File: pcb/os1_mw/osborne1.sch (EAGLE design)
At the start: 19 parts

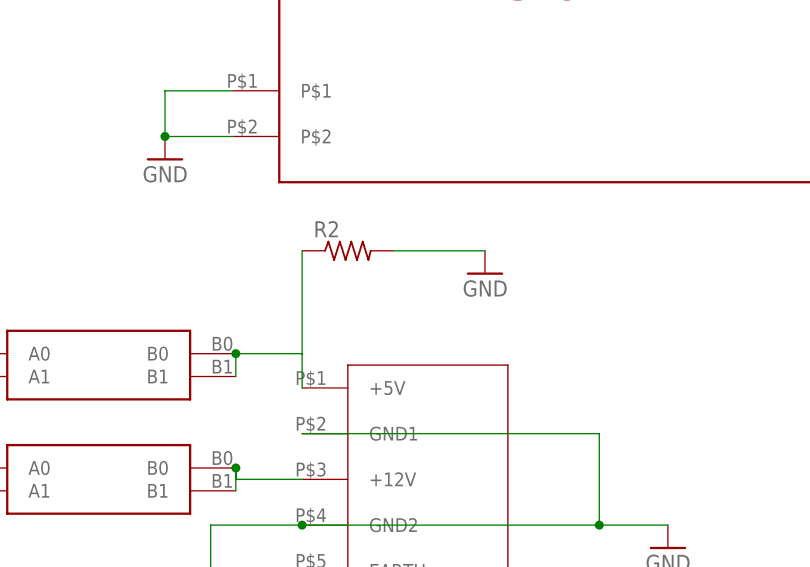
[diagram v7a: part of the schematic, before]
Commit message: update os1 pcb
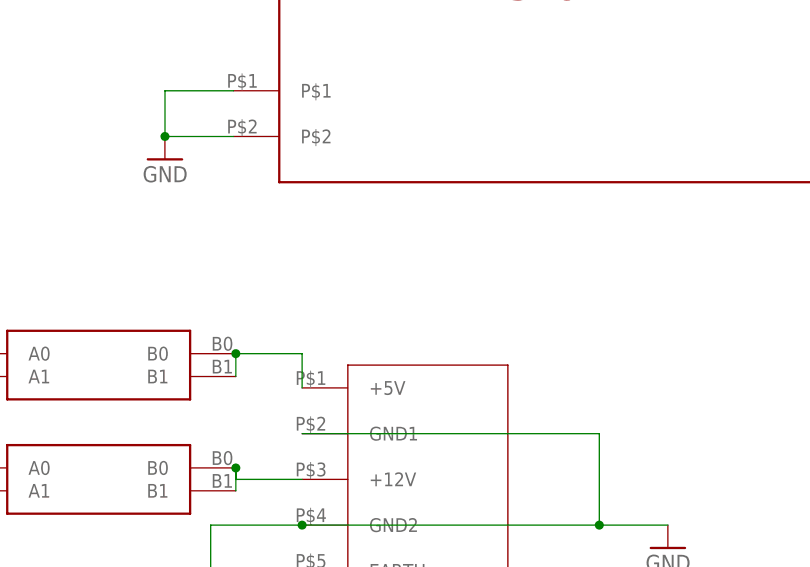
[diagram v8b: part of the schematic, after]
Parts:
- removed R2: (no value), adafruit_changed:R-US_0411/15
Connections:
- net GND: no longer R2.2
- net N$2: no longer R2.1
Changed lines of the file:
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@@
 <part name="P+10" library="supply1" library_urn="urn:adsk.eagle:library:371" deviceset="+12V" device=""/>
 <part name="GND1" library="supply1" library_urn="urn:adsk.eagle:library:371" deviceset="GND" device=""/>
-<part name="R2" library="adafruit_changed" deviceset="R-US_" device="0411/15"/>
-<part name="GND3" library="supply1" library_urn="urn:adsk.eagle:library:371" deviceset="GND" device=""/>
 <part name="GND5" library="supply1" library_urn="urn:adsk.eagle:library:371" deviceset="GND" device=""/>
 <part name="U$3" library="os1" deviceset="TERM_RD50_MAINS" device=""/>
@@
 <instance part="GND1" gate="1" x="27.94" y="99.06" smashed="yes" rot="MR0">
 <attribute name="VALUE" x="30.48" y="96.52" size="1.778" layer="96" rot="MR0"/>
-</instance>
-<instance part="R2" gate="G$1" x="20.32" y="2.54" smashed="yes">
-<attribute name="NAME" x="16.51" y="4.0386" size="1.778" layer="95"/>
-<attribute name="VALUE" x="16.51" y="-0.762" size="1.778" layer="96"/>
-</instance>
-<instance part="GND3" gate="1" x="35.56" y="0" smashed="yes" rot="MR0">
-<attribute name="VALUE" x="38.1" y="-2.54" size="1.778" layer="96" rot="MR0"/>
 </instance>
 <instance part="GND5" gate="1" x="0" y="12.7" smashed="yes" rot="MR0">
@@
 </segment>
 <segment>
-<pinref part="GND3" gate="1" pin="GND"/>
-<pinref part="R2" gate="G$1" pin="2"/>
-<wire x1="35.56" y1="2.54" x2="25.4" y2="2.54" width="0.1524" layer="91"/>
-</segment>
-<segment>
 <pinref part="U$1" gate="G$1" pin="P$2"/>
 <pinref part="GND5" gate="1" pin="GND"/>
@@
 <wire x1="15.24" y1="-8.89" x2="7.874" y2="-8.89" width="0.1524" layer="91"/>
 <junction x="7.874" y="-8.89"/>
-<pinref part="R2" gate="G$1" pin="1"/>
-<wire x1="15.24" y1="2.54" x2="15.24" y2="-8.89" width="0.1524" layer="91"/>
 <pinref part="U$3" gate="G$1" pin="+5V"/>
 </segment>
